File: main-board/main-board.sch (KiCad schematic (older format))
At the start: 18 parts, among them J1 C10418, J2 FH12-24S-0.5SH(55), U1 ESP-32s, U2 HT7333-A, U3 CH340E

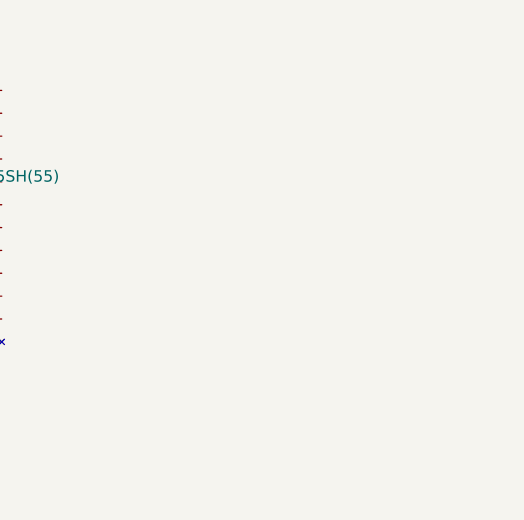
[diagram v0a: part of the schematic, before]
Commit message: battery holder
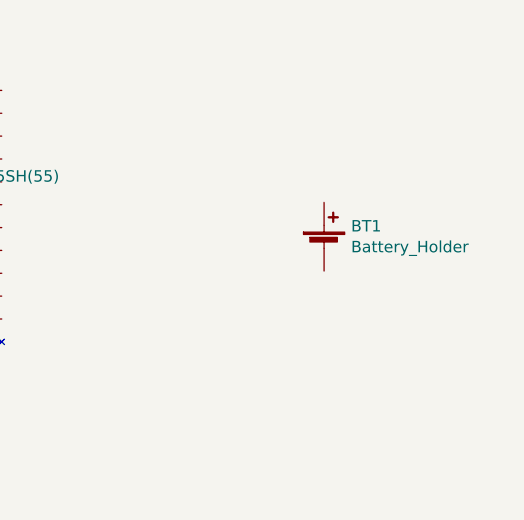
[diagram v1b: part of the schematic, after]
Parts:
- added BT1: Battery_Holder, water-lib:Battery Holder SMD, symbol water-lib:Battery_Holder
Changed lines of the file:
@@
 VCC
 $Comp
-L power:GND #PWR?
+L power:GND #PWR015
 U 1 1 5D9C0A97
 P 1700 6200
-F 0 "#PWR?" H 1700 5950 50  0001 C CNN
+F 0 "#PWR015" H 1700 5950 50  0001 C CNN
 F 1 "GND" H 1705 6027 50  0000 C CNN
 F 2 "" H 1700 6200 50  0001 C CNN
@@
 	1700 6000 1700 5900
 Connection ~ 1700 6000
+$Comp
+L water-lib:Battery_Holder BT1
+U 1 1 5D9F0EFE
+P 7760 1790
+F 0 "BT1" H 7878 1886 50  0000 L CNN
+F 1 "Battery_Holder" H 7878 1795 50  0000 L CNN
+F 2 "water-lib:Battery Holder SMD" V 7590 1850 50  0001 C CNN
+F 3 "~" V 7760 1850 50  0001 C CNN
+	1    7760 1790
+	1    0    0    -1
+$EndComp
 $EndSCHEMATC

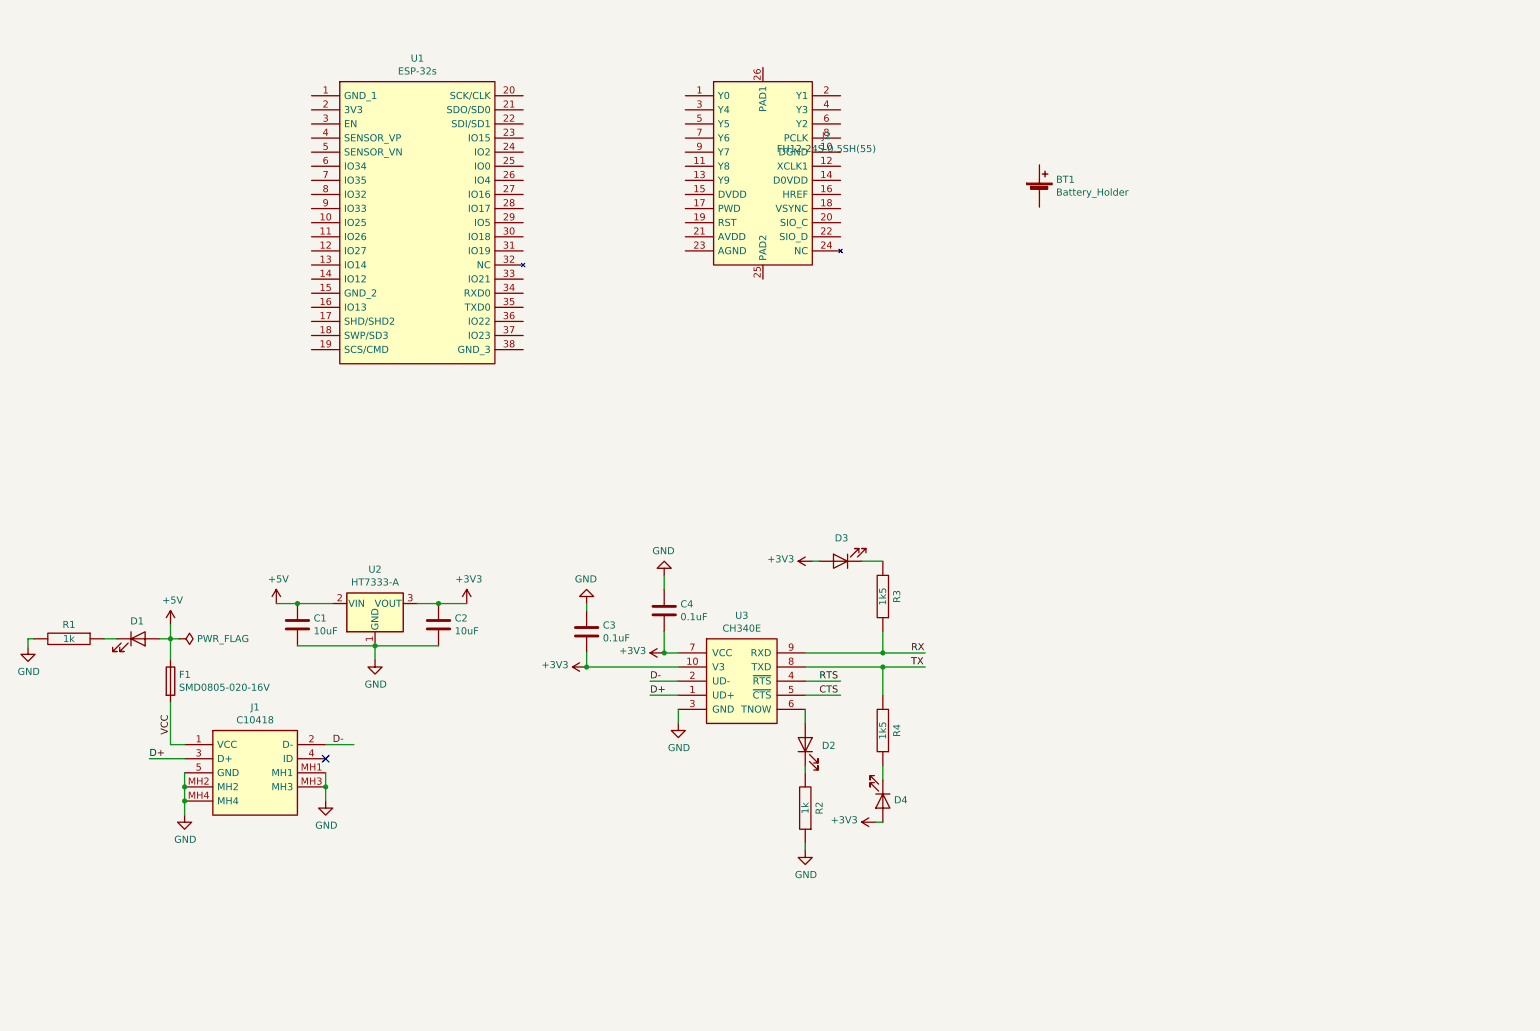
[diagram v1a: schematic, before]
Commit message: battery protection + buckboost
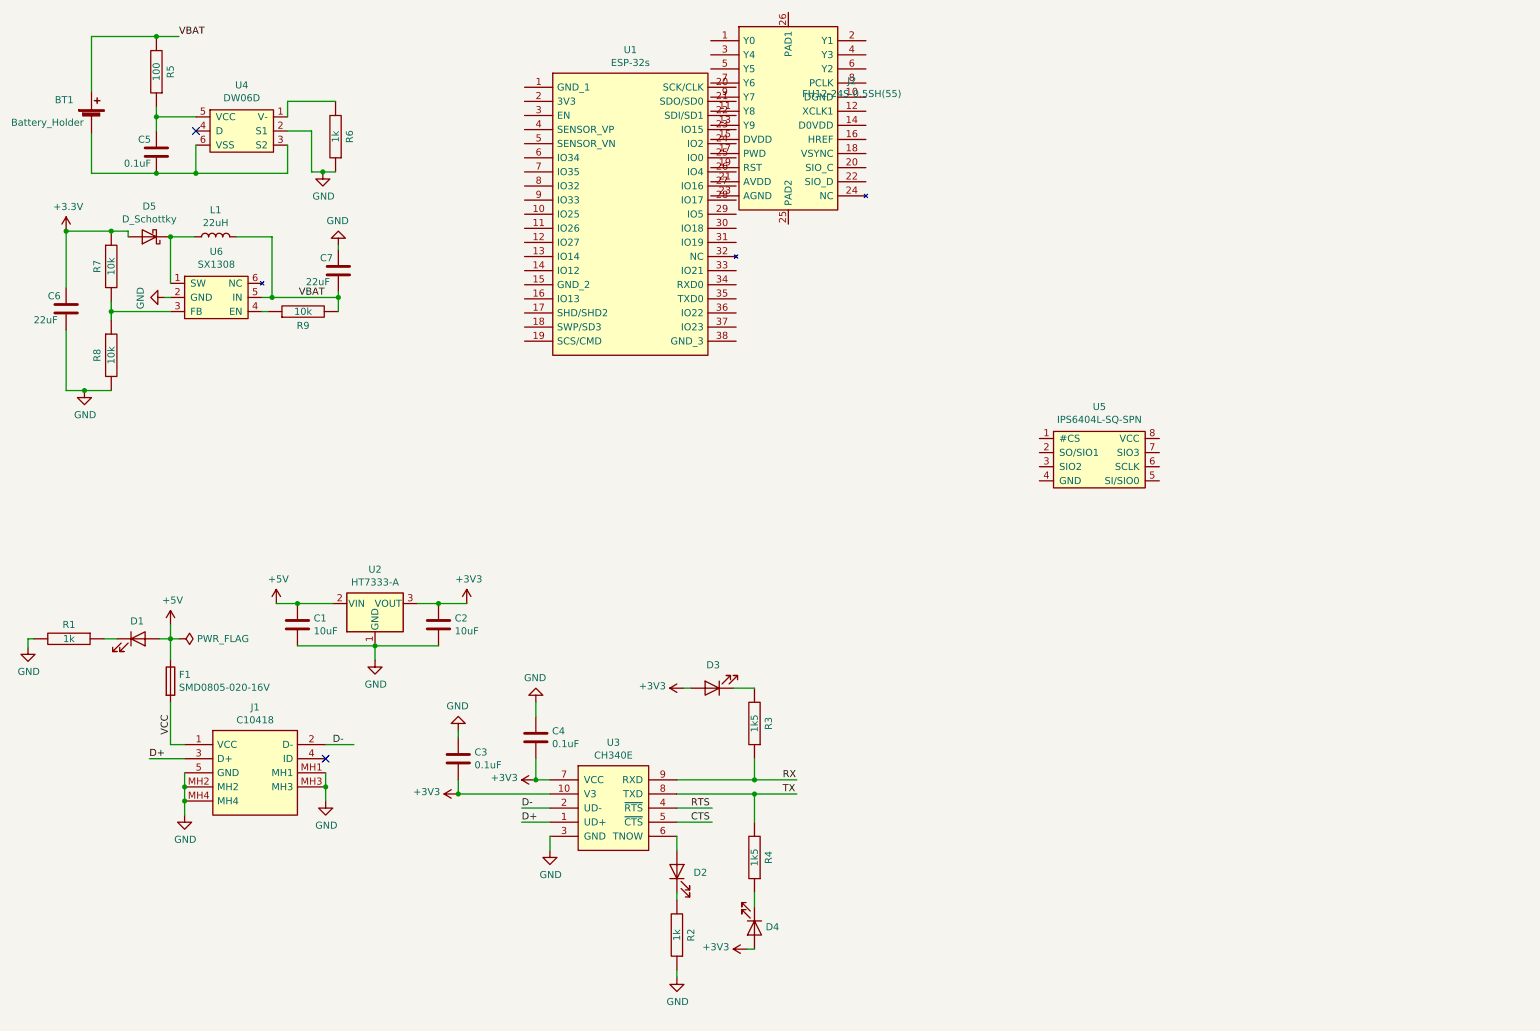
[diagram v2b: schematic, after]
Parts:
- added C5: 0.1uF, Capacitor_SMD:C_0805_2012Metric_Pad1.15x1.40mm_HandSolder, symbol Device:C
- added C6, C7: 22uF, Capacitor_SMD:C_0805_2012Metric_Pad1.15x1.40mm_HandSolder, symbol Device:C
- added D5: D_Schottky, Diode_SMD:D_0805_2012Metric_Pad1.15x1.40mm_HandSolder, symbol Device:D_Schottky
- added L1: 22uH, Inductor_SMD:L_6.3x6.3_H3, symbol Device:L
- added R5: 100, Resistor_SMD:R_0805_2012Metric_Pad1.15x1.40mm_HandSolder, symbol pspice:R
- added R6: 1k, Resistor_SMD:R_0805_2012Metric_Pad1.15x1.40mm_HandSolder, symbol pspice:R
- added R7, R8, R9: 10k, Resistor_SMD:R_0805_2012Metric_Pad1.15x1.40mm_HandSolder, symbol pspice:R
- added U4: DW06D, Package_TO_SOT_SMD:SOT-23-6_Handsoldering, symbol water-lib:DW06D
- added U5: IPS6404L-SQ-SPN, Package_SO:SOP-8_3.76x4.96mm_P1.27mm, symbol water-lib:IPS6404L-SQ-SPN
- added U6: SX1308, Package_TO_SOT_SMD:SOT-23-6_Handsoldering, symbol water-lib:SX1308
- BT1: footprint water-lib:Battery Holder SMD -> water-lib:Battery-Holder-SMD
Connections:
- net labels added: +3.3V, VBAT
- wire segments 47 -> 86
- no-connect marks 1 -> 2
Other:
- moved on the sheet: C3, C4, D2, D3, D4, J2, R2, R3, R4, U1, U3

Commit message: boost, LDOs, ribbon connerctions
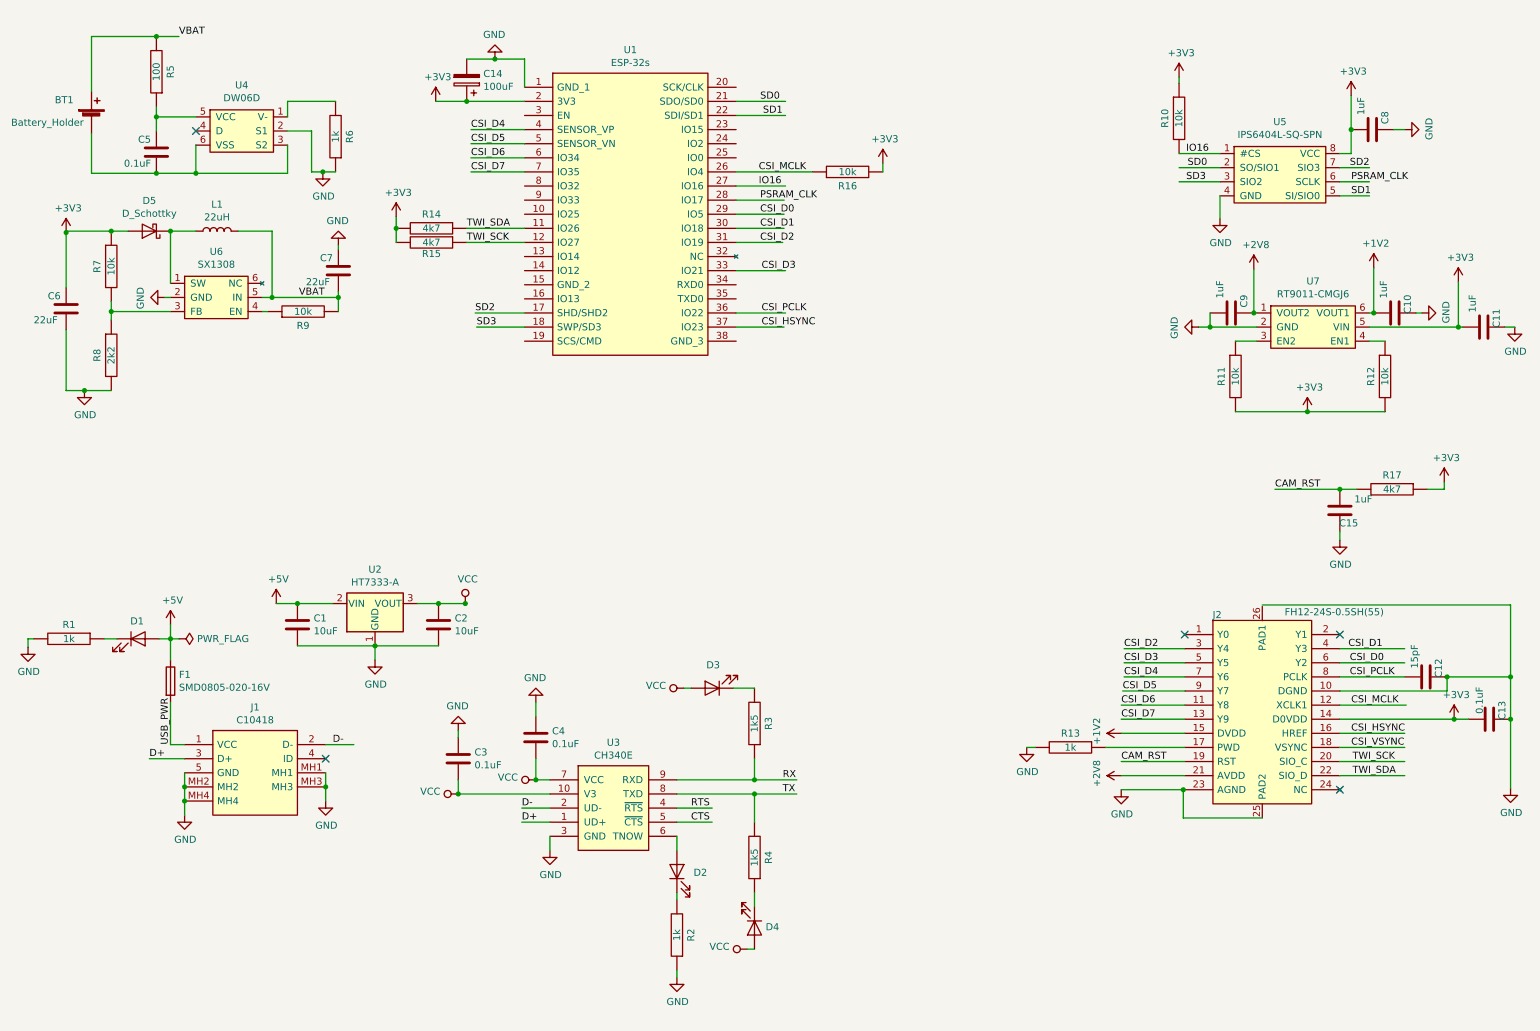
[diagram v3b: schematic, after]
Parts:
- added C10, C11, C15, C8, C9: 1uF, Capacitor_SMD:C_0805_2012Metric_Pad1.15x1.40mm_HandSolder, symbol Device:C
- added C12: 15pF, Capacitor_SMD:C_0805_2012Metric_Pad1.15x1.40mm_HandSolder, symbol Device:C
- added C13: 0.1uF, Capacitor_SMD:C_0805_2012Metric_Pad1.15x1.40mm_HandSolder, symbol Device:C
- added C14: 100uF, water-lib:TAJB107M010RNJ, symbol Device:CP
- added R10, R11, R12, R16: 10k, Resistor_SMD:R_0805_2012Metric_Pad1.15x1.40mm_HandSolder, symbol pspice:R
- added R13: 1k, Resistor_SMD:R_0805_2012Metric_Pad1.15x1.40mm_HandSolder, symbol pspice:R
- added R14, R15, R17: 4k7, Resistor_SMD:R_0805_2012Metric_Pad1.15x1.40mm_HandSolder, symbol pspice:R
- added U7: RT9011-CMGJ6, Package_TO_SOT_SMD:SOT-23-6_Handsoldering, symbol water-lib:RT9011-CMGJ6
- R8: value 10k -> 2k2
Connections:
- net labels added: +1V2, +2V8, CAM_RST, CSI_D0, CSI_D1, CSI_D2, CSI_D3, CSI_D4, CSI_D5, CSI_D6, CSI_D7, CSI_HSYNC, CSI_MCLK, CSI_PCLK, CSI_VSYNC, IO16, PSRAM_CLK, SD0, SD1, SD2, SD3, TWI_SCK, TWI_SDA, USB_PWR
- net labels removed: +3.3V
- wire segments 86 -> 180
- no-connect marks 2 -> 5
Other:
- moved on the sheet: D5, J2, L1, U5

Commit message: ribbon connections and reset sw
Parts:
- added R18: 10k, Resistor_SMD:R_0805_2012Metric_Pad1.15x1.40mm_HandSolder, symbol pspice:R
- added SW1: SW_DIP_x01, Button_Switch_SMD:SW_SPST_CK_RS282G05A3, symbol Switch:SW_DIP_x01
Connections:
- net labels added: CSI_PWD, EN
- wire segments 180 -> 186
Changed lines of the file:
@@
 Wire Wire Line
 	3200 2040 3200 1960
+Wire Wire Line
+	4110 1940 3700 1940
+Text Label 3700 1940 0    50   ~ 0
+CSI_VSYNC
+Text Label 8340 5720 0    50   ~ 0
+CSI_PWD
+$Comp
+L Switch:SW_DIP_x01 SW1
+U 1 1 5DA39DF7
+P 6760 5130
+F 0 "SW1" H 6760 5397 50  0000 C CNN
+F 1 "SW_DIP_x01" H 6760 5306 50  0000 C CNN
+F 2 "Button_Switch_SMD:SW_SPST_CK_RS282G05A3" H 6760 5130 50  0001 C CNN
+F 3 "~" H 6760 5130 50  0001 C CNN
+	1    6760 5130
+	1    0    0    -1
+$EndComp
+$Comp
+L power:GND #PWR0101
+U 1 1 5DA3B5A0
+P 6350 5130
+F 0 "#PWR0101" H 6350 4880 50  0001 C CNN
+F 1 "GND" H 6355 4957 50  0000 C CNN
+F 2 "" H 6350 5130 50  0001 C CNN
+F 3 "" H 6350 5130 50  0001 C CNN
+	1    6350 5130
+	1    0    0    -1
+$EndComp
+Wire Wire Line
+	7060 5130 7290 5130
+Wire Wire Line
+	6460 5130 6350 5130
+Wire Wire Line
+	4110 1240 3740 1240
+Text Label 3740 1240 0    50   ~ 0
+EN
+Text Label 7590 5130 0    50   ~ 0
+EN
+$Comp
+L pspice:R R18
+U 1 1 5DA63BFF
+P 7290 4880
+F 0 "R18" V 7190 4880 50  0000 C CNN
+F 1 "10k" V 7290 4880 50  0000 C CNN
+F 2 "Resistor_SMD:R_0805_2012Metric_Pad1.15x1.40mm_HandSolder" H 7290 4880 50  0001 C CNN
+F 3 "~" H 7290 4880 50  0001 C CNN
+	1    7290 4880
+	1    0    0    -1
+$EndComp
+Connection ~ 7290 5130
+Wire Wire Line
+	7290 5130 7720 5130
+$Comp
+L power:+3V3 #PWR0102
+U 1 1 5DA640C1
+P 7290 4570
+F 0 "#PWR0102" H 7290 4420 50  0001 C CNN
+F 1 "+3V3" H 7305 4743 50  0000 C CNN
+F 2 "" H 7290 4570 50  0001 C CNN
+F 3 "" H 7290 4570 50  0001 C CNN
+	1    7290 4570
+	1    0    0    -1
+$EndComp
+Wire Wire Line
+	7290 4570 7290 4630
 $EndSCHEMATC

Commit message: SD card
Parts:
- added J3: TF-01A, water-lib:TF-01A, symbol water-lib:TF-01A
- added Q1, Q2: Q_NPN_BCE, Package_TO_SOT_SMD:SOT-23, symbol Device:Q_NPN_BCE
- added R19, R20: 10k, Resistor_SMD:R_0805_2012Metric_Pad1.15x1.40mm_HandSolder, symbol pspice:R
- added U8: SN74LVC125ADBR, Package_SO:TSSOP-14_4.4x5mm_P0.65mm, symbol water-lib:SN74LVC125ADBR
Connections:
- net labels added: IO0
- wire segments 186 -> 201
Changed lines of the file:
@@
 Wire Wire Line
 	7290 4570 7290 4630
+Wire Wire Line
+	5610 2440 5960 2440
+Wire Wire Line
+	5610 2540 5960 2540
+Text Label 5800 2440 0    50   ~ 0
+TX
+Text Label 5810 2540 0    50   ~ 0
+RX
+Wire Wire Line
+	5610 1540 5980 1540
+Text Label 5780 1540 0    50   ~ 0
+IO0
+$Comp
+L Device:Q_NPN_BCE Q1
+U 1 1 5D9CDA07
+P 2740 6850
+F 0 "Q1" H 2931 6896 50  0000 L CNN
+F 1 "Q_NPN_BCE" H 2931 6805 50  0000 L CNN
+F 2 "Package_TO_SOT_SMD:SOT-23" H 2940 6950 50  0001 C CNN
+F 3 "https://lcsc.com/product-detail/Transistors-NPN-PNP_BC847B_C181140.html" H 2740 6850 50  0001 C CNN
+F 4 "C181140" H 2740 6850 50  0001 C CNN "LCSC"
+	1    2740 6850
+	1    0    0    -1
+$EndComp
+$Comp
+L Device:Q_NPN_BCE Q2
+U 1 1 5D9CE8C6
+P 2740 7440
+F 0 "Q2" H 2931 7486 50  0000 L CNN
+F 1 "Q_NPN_BCE" H 2931 7395 50  0000 L CNN
+F 2 "Package_TO_SOT_SMD:SOT-23" H 2940 7540 50  0001 C CNN
+F 3 "https://lcsc.com/product-detail/Transistors-NPN-PNP_BC847B_C181140.html" H 2740 7440 50  0001 C CNN
+F 4 "C181140" H 2740 7440 50  0001 C CNN "LCSC"
+	1    2740 7440
+	1    0    0    -1
+$EndComp
+$Comp
+L pspice:R R20
+U 1 1 5D9D3A82
+P 2200 7440
+F 0 "R20" V 2100 7440 50  0000 C CNN
+F 1 "10k" V 2200 7440 50  0000 C CNN
+F 2 "Resistor_SMD:R_0805_2012Metric_Pad1.15x1.40mm_HandSolder" H 2200 7440 50  0001 C CNN
+F 3 "~" H 2200 7440 50  0001 C CNN
+	1    2200 7440
+	0    1    1    0
+$EndComp
+$Comp
+L pspice:R R19
+U 1 1 5D9D15D2
+P 2200 6850
+F 0 "R19" V 2100 6850 50  0000 C CNN
+F 1 "10k" V 2200 6850 50  0000 C CNN
+F 2 "Resistor_SMD:R_0805_2012Metric_Pad1.15x1.40mm_HandSolder" H 2200 6850 50  0001 C CNN
+F 3 "~" H 2200 6850 50  0001 C CNN
+	1    2200 6850
+	0    1    1    0
+$EndComp
+Wire Wire Line
+	1950 6850 1700 6850
+Wire Wire Line
+	1950 7440 1850 7440
+Text Label 1700 6850 0    50   ~ 0
+RTS
+Text Label 1690 7440 0    50   ~ 0
+CTS
+Wire Wire Line
+	2450 6850 2540 6850
+Wire Wire Line
+	2840 6650 3130 6650
+Text Label 3010 6650 0    50   ~ 0
+IO0
+Text Label 2960 7640 0    50   ~ 0
+EN
+Wire Wire Line
+	2840 7640 3210 7640
+Connection ~ 1950 6850
+Wire Wire Line
+	2450 7440 2540 7440
+Wire Wire Line
+	1950 7150 2840 7150
+Wire Wire Line
+	2840 7150 2840 7240
+Wire Wire Line
+	1950 6850 1950 7150
+Wire Wire Line
+	2840 7050 1850 7050
+Wire Wire Line
+	1850 7050 1850 7440
+Connection ~ 1850 7440
+Wire Wire Line
+	1850 7440 1690 7440
+$Comp
+L water-lib:TF-01A J3
+U 1 1 5D9D5E7E
+P 2310 3530
+F 0 "J3" H 2260 4255 50  0000 C CNN
+F 1 "TF-01A" H 2260 4164 50  0000 C CNN
+F 2 "water-lib:TF-01A" H 3460 3830 50  0001 C CNN
+F 3 "https://datasheet.lcsc.com/szlcsc/1903221101_Korean-Hroparts-Elec-TF-01A_C91145.pdf" H 2310 3530 50  0001 C CNN
+F 4 "C91145" H 2310 3530 50  0001 C CNN "LCSC"
+	1    2310 3530
+	1    0    0    -1
+$EndComp
+$Comp
+L water-lib:SN74LVC125ADBR U8
+U 1 1 5DA00509
+P 3950 3730
+F 0 "U8" H 3950 4511 50  0000 C CNN
+F 1 "SN74LVC125ADBR" H 3950 4420 50  0000 C CNN
+F 2 "Package_SO:TSSOP-14_4.4x5mm_P0.65mm" H 4900 3180 50  0001 C CNN
+F 3 "https://datasheet.lcsc.com/szlcsc/Texas-Instruments-TI-SN74LVC125ADBR_C7812.pdf" H 3950 3730 50  0001 C CNN
+F 4 "C7812" H 4200 3280 50  0001 C CNN "LCSC"
+	1    3950 3730
+	1    0    0    -1
+$EndComp
 $EndSCHEMATC
